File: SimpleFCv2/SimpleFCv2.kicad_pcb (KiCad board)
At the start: 4 copper layers, 42 x 50 mm, 126 parts, among them J1 M02, J10 USB_B_Micro, J11 M04, J12 Conn_SWD, J13 MOUNTING_HOLE, J14 MOUNTING_HOLE, J15 MOUNTING_HOLE, J16 MOUNTING_HOLE, J2 Micro_SD_Card_Det, J3 M04, J4 M04, J5 M10, J6 M10, J7 M10, J8 M03, J9 M04, Q1 AO3407A, Q2 AO6802, U1 STM32F405RGT6, U10 74LVC1G86, U11 TJA1050, U2 MS5611, U3 MAG3110, U4 ICM-20689, U5 MP2403, U6 SPX3819M5, U7 AT24C512C, U8 74LVC1G86, U9 SN74LVC245, X1 25Mhz

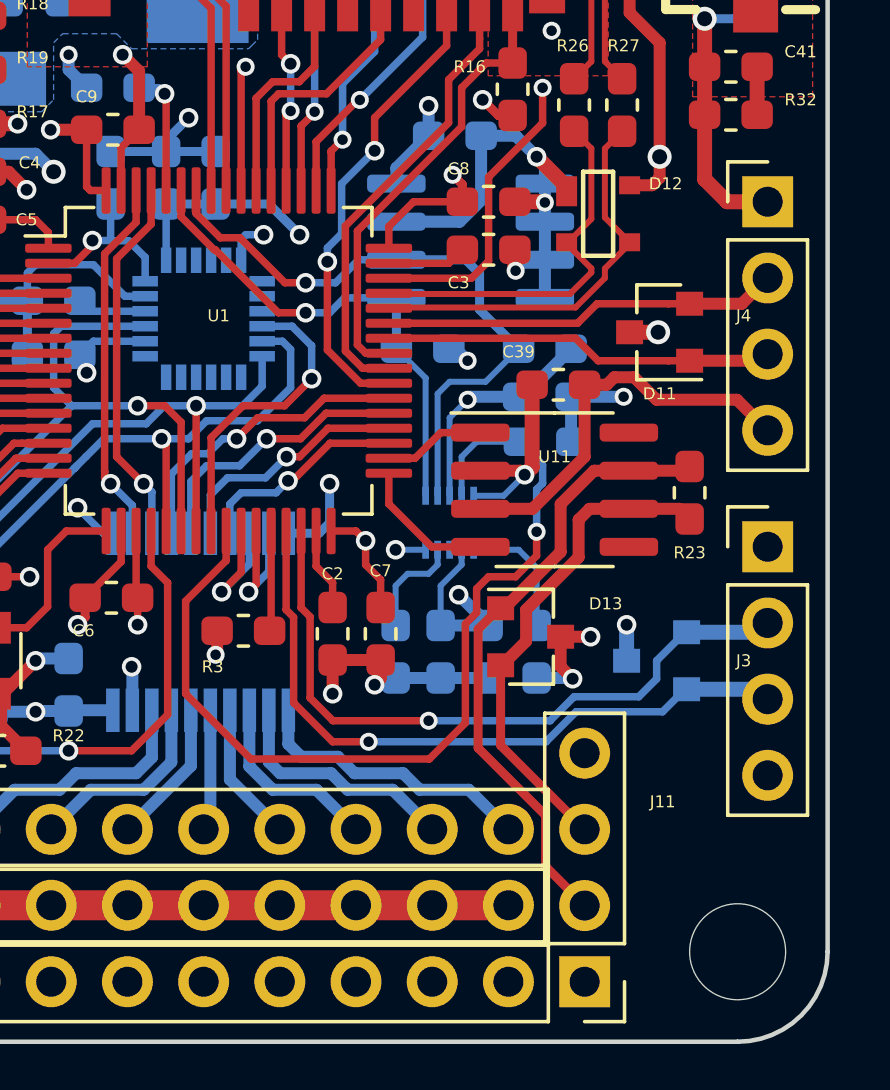
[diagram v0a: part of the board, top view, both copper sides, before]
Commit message: Replace MAG3110 with MMC5883MA in SimpleFC
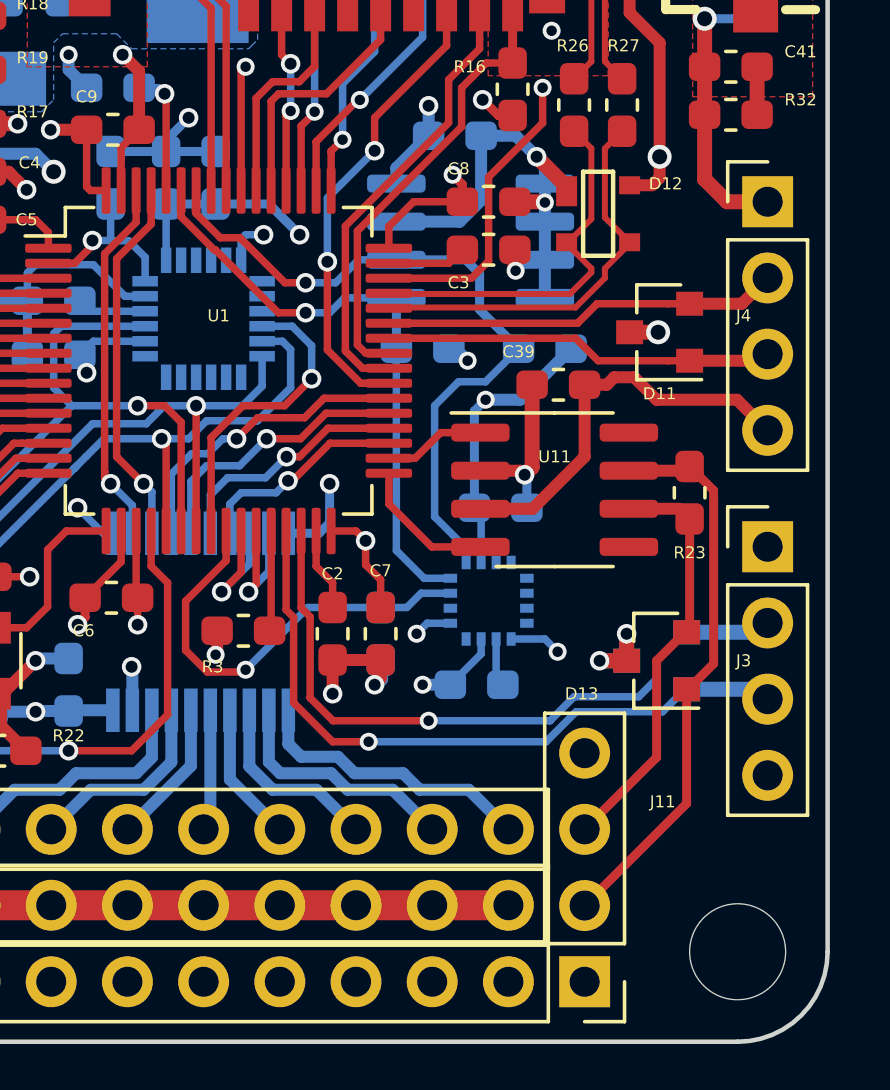
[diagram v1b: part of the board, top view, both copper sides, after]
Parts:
- removed C12, C16, C17: 100nF, Capacitor_SMD:C_0603_1608Metric_Pad1.05x0.95mm_HandSolder
- C15: value 100nF -> 10uF
- U3: value MAG3110 -> MMC5883MA; footprint MEMS:DFN-10 -> Package_LGA:LGA-16_3x3mm_P0.5mm
- moved R7 8.44 mm to (153.1, 109.4), turned to 270 degrees
- moved C14 5.20 mm to (157.1, 105.2), turned to 0 degrees
- moved D13 4.28 mm to (162.3, 110.3), turned to 180 degrees
- moved U3 2.91 mm to (156.7, 108.3), turned to 270 degrees
- moved C15 1.17 mm to (156.3, 111.1), turned to 180 degrees
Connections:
- C15 pad 1: +3V3 -> Net-(C15-Pad1)
- U3 pad 1: Net-(C16-Pad1) -> I2C1_SCL
- U3 pad 10: GND -> Net-(C15-Pad1)
- U3 pad 5: GND -> Net-(U3-Pad5)
- U3 pad 6: I2C1_SDA -> Net-(U3-Pad6)
- U3 pad 7: I2C1_SCL -> Net-(U3-Pad7)
- U3 pad 8: +3V3 -> Net-(U3-Pad8)
- U3 pad 9: MAG_INT -> GND
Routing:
- net MAG_INT: track 31.4 -> 14.7 mm
- net GND: track 175.0 -> 170.1 mm, vias 56 -> 55
- net Net-(C16-Pad1): track 4.27 -> 0.00 mm
- net I2C1_SDA: track 16.6 -> 20.3 mm
- net Net-(U3-Pad4): track 3.51 -> 0.00 mm
- net +3V3: track 80.3 -> 77.4 mm
- net CANL: track 16.6 -> 14.0 mm
- net I2C1_SCL: track 21.4 -> 24.0 mm
- net CANH: track 21.0 -> 18.9 mm
- net Net-(C15-Pad1): track 0.00 -> 1.62 mm
